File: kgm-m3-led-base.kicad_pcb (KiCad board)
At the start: 2 copper layers, 22.2 x 50.8 mm, 24 parts, among them J1 Conn_02x06_Counter_Clockwise

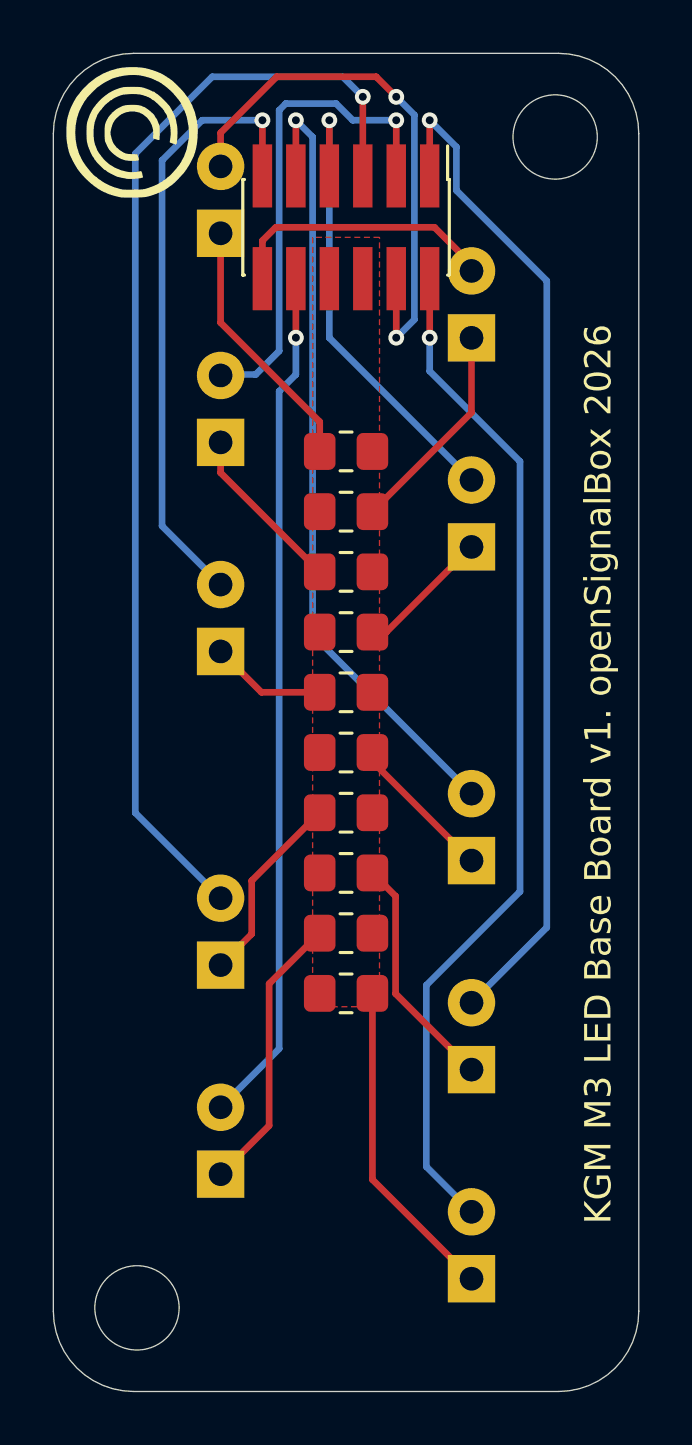
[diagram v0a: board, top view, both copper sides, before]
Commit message: Added fiducials to PCB and updated silk to add .org
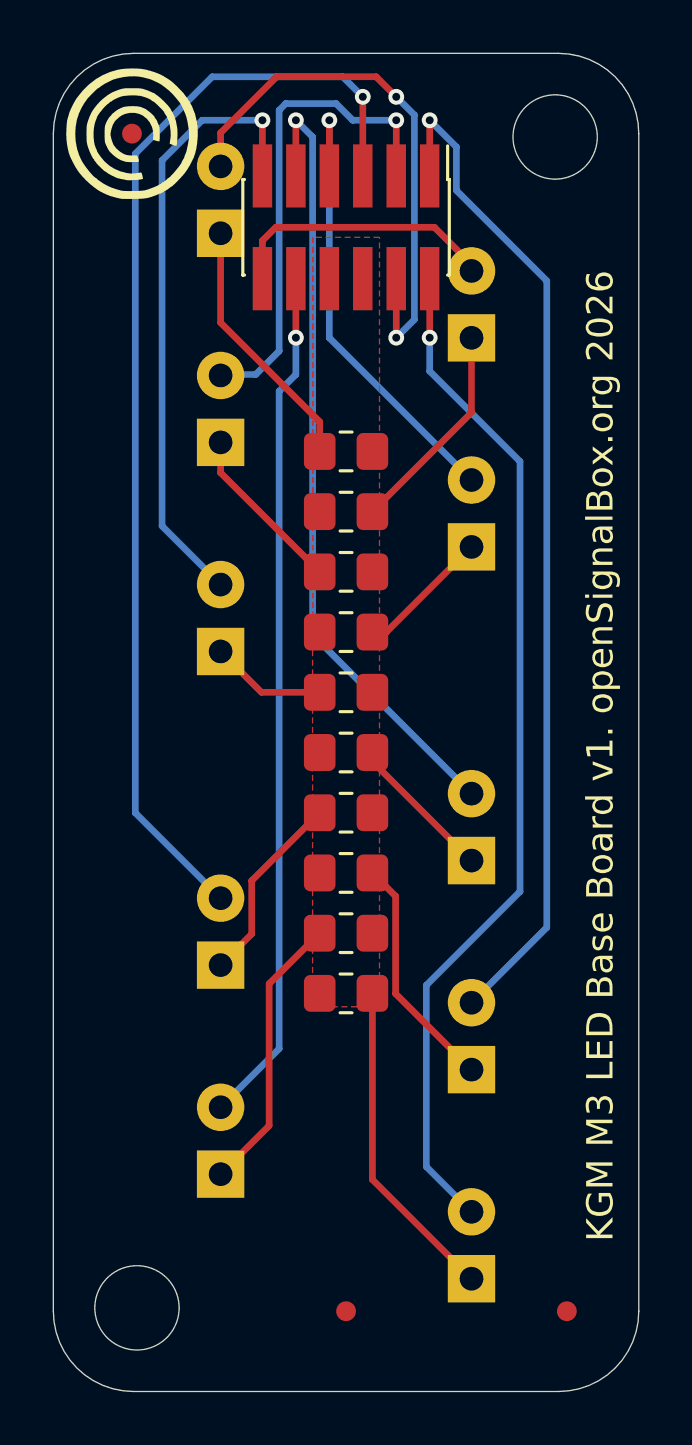
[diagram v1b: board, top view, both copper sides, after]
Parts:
- added FID1: Fiducial, Fiducial:Fiducial_0.75mm_Mask1.5mm, F.Cu at (144.3, 79.2)
- added FID2: Fiducial, Fiducial:Fiducial_0.75mm_Mask1.5mm, F.Cu at (160.8, 124.0)
- added FID3: Fiducial, Fiducial:Fiducial_0.75mm_Mask1.5mm, F.Cu at (152.4, 124.0)
- moved G*** 0.05 mm to (144.3, 79.2)
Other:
- board text added: "KGM M3 LED Base Board v1. openSignalBox.org 2026"
- board text removed: "KGM M3 LED Base Board v1. openSignalBox 2026"

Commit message: Redesigned connector, added spacer model
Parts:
- added J2: Conn_02x03_Counter_Clockwise, Connector_PinHeader_2.54mm:PinHeader_2x03_P2.54mm_Vertical_SMD, F.Cu at (152.4, 120.4)
- J1: value Conn_02x06_Counter_Clockwise -> Conn_02x03_Counter_Clockwise; footprint Connector_PinHeader_1.27mm:PinHeader_2x06_P1.27mm_Vertical_SMD -> Connector_PinHeader_2.54mm:PinHeader_2x03_P2.54mm_Vertical_SMD
- moved FID3 23.8 mm to (144.3, 101.6)
- turned J1 to 90 degrees
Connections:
- J1 pad 1: Net-(D6-A) -> Net-(D5-A)
- J1 pad 2: Net-(D10-A) -> Net-(D9-A)
- J1 pad 3: Net-(D5-A) -> /COM
- J1 pad 4: Net-(D9-A) -> Net-(D1-A)
- J1 pad 5: Net-(D4-A) -> Net-(D3-A)
- J1 pad 6: /COM -> Net-(D7-A)
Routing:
- net Net-(D10-A): track 39.0 -> 4.69 mm, vias 1 -> 0
- net Net-(D4-A): track 42.8 -> 10.5 mm, vias 1 -> 0
- net Net-(D6-A): track 38.6 -> 7.17 mm, vias 1 -> 0
- net Net-(D8-A): track 32.6 -> 15.4 mm, vias 1 -> 0
- net Net-(D9-A): track 21.1 -> 5.75 mm, vias 2 -> 0
- net Net-(D5-A): track 18.7 -> 4.85 mm, vias 1 -> 0
- net Net-(D3-A): track 18.0 -> 7.99 mm, vias 1 -> 0
- net Net-(D10-K): track 12.4 -> 19.4 mm
- net Net-(D8-K): track 10.7 -> 16.3 mm
- net Net-(D7-A): track 10.4 -> 5.10 mm
- net Net-(D1-A): track 23.6 -> 28.1 mm, vias 1 -> 0
- net Net-(D7-K): track 8.16 -> 12.4 mm
- net Net-(D4-K): track 7.34 -> 11.2 mm
- net Net-(D9-K): track 9.84 -> 12.6 mm
- net Net-(D6-K): track 9.02 -> 11.6 mm
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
